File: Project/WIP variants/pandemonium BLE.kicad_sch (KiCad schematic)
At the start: 117 parts, among them J1 HRO_TYPE-C-31-M-14, J3 Battery, J7 TC2030_SWD, Q1 AO3407, SW1 RotaryEncoder_Switch, SW2 RotaryEncoder_Switch, U2 HOLYIOT-18010, U3 MCP73831, U4 USBLC6-2P6, U8 XC6206PxxxMR

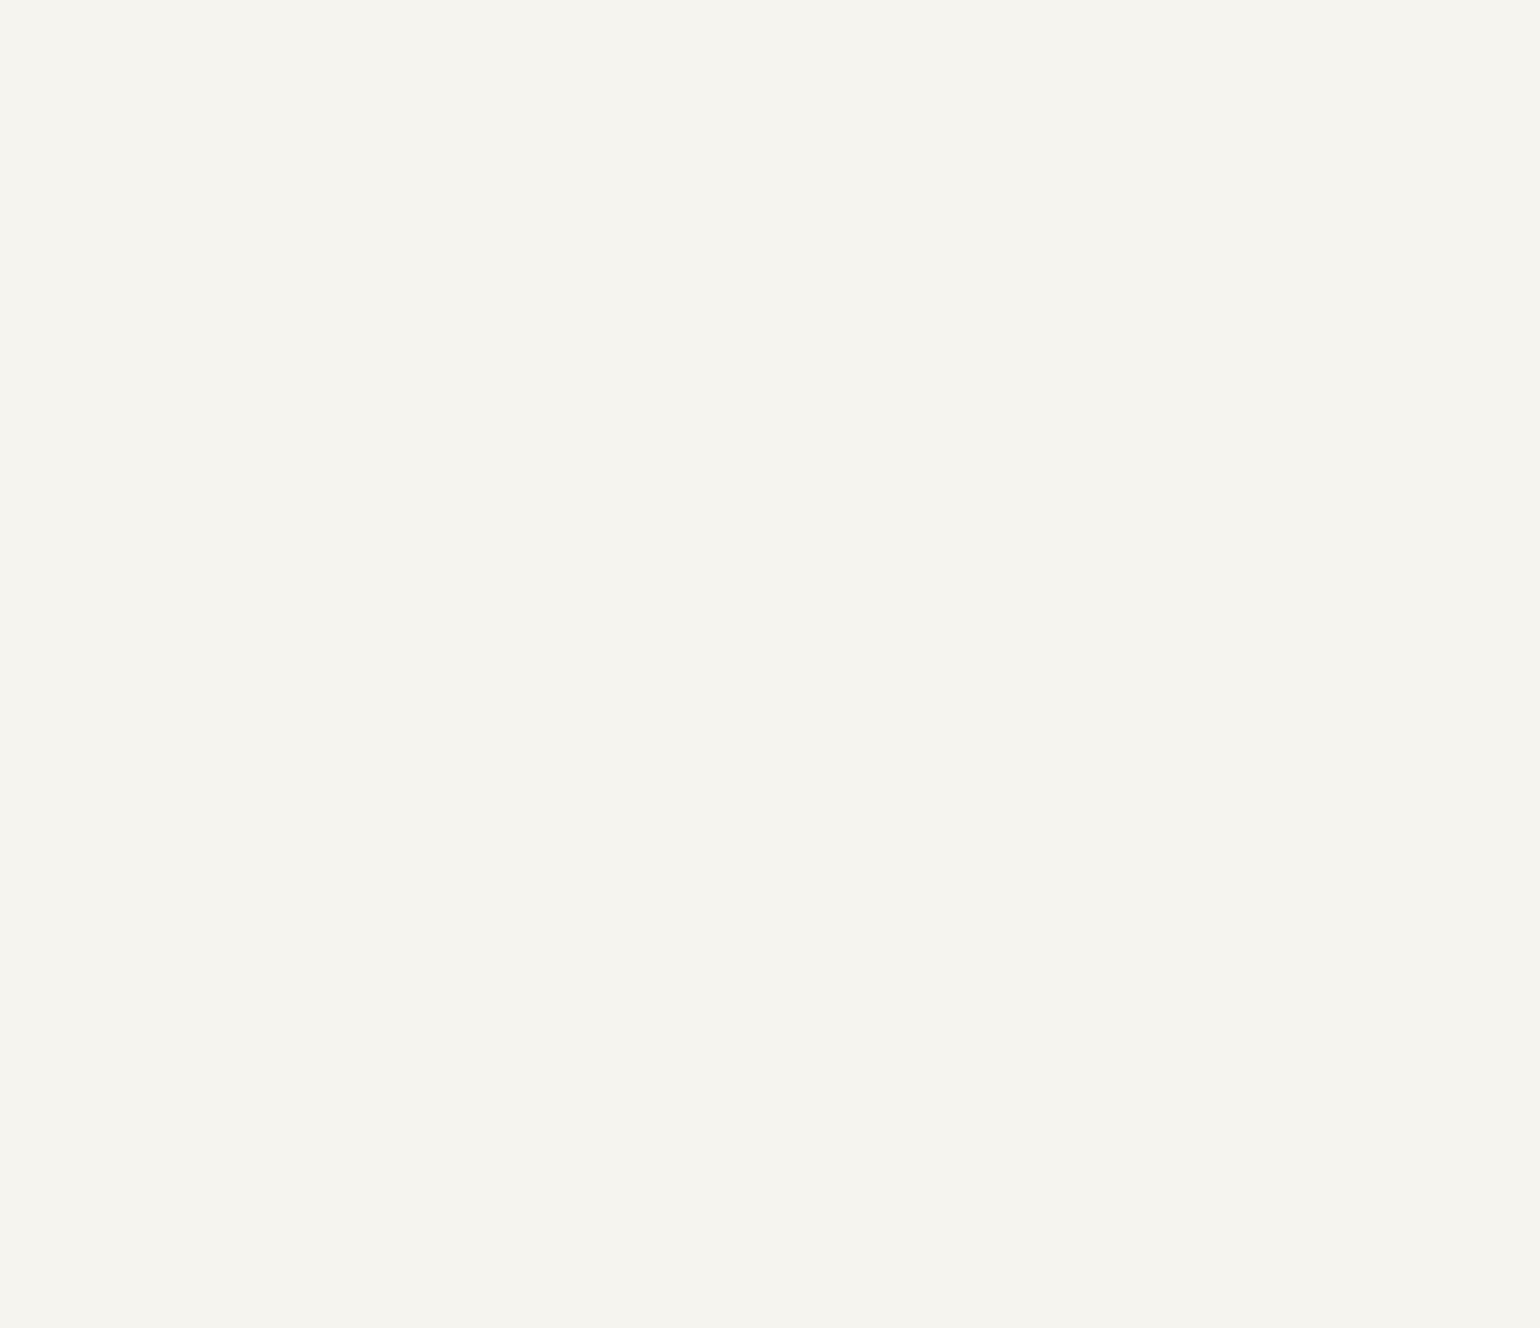
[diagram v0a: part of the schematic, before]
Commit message: e73 version work
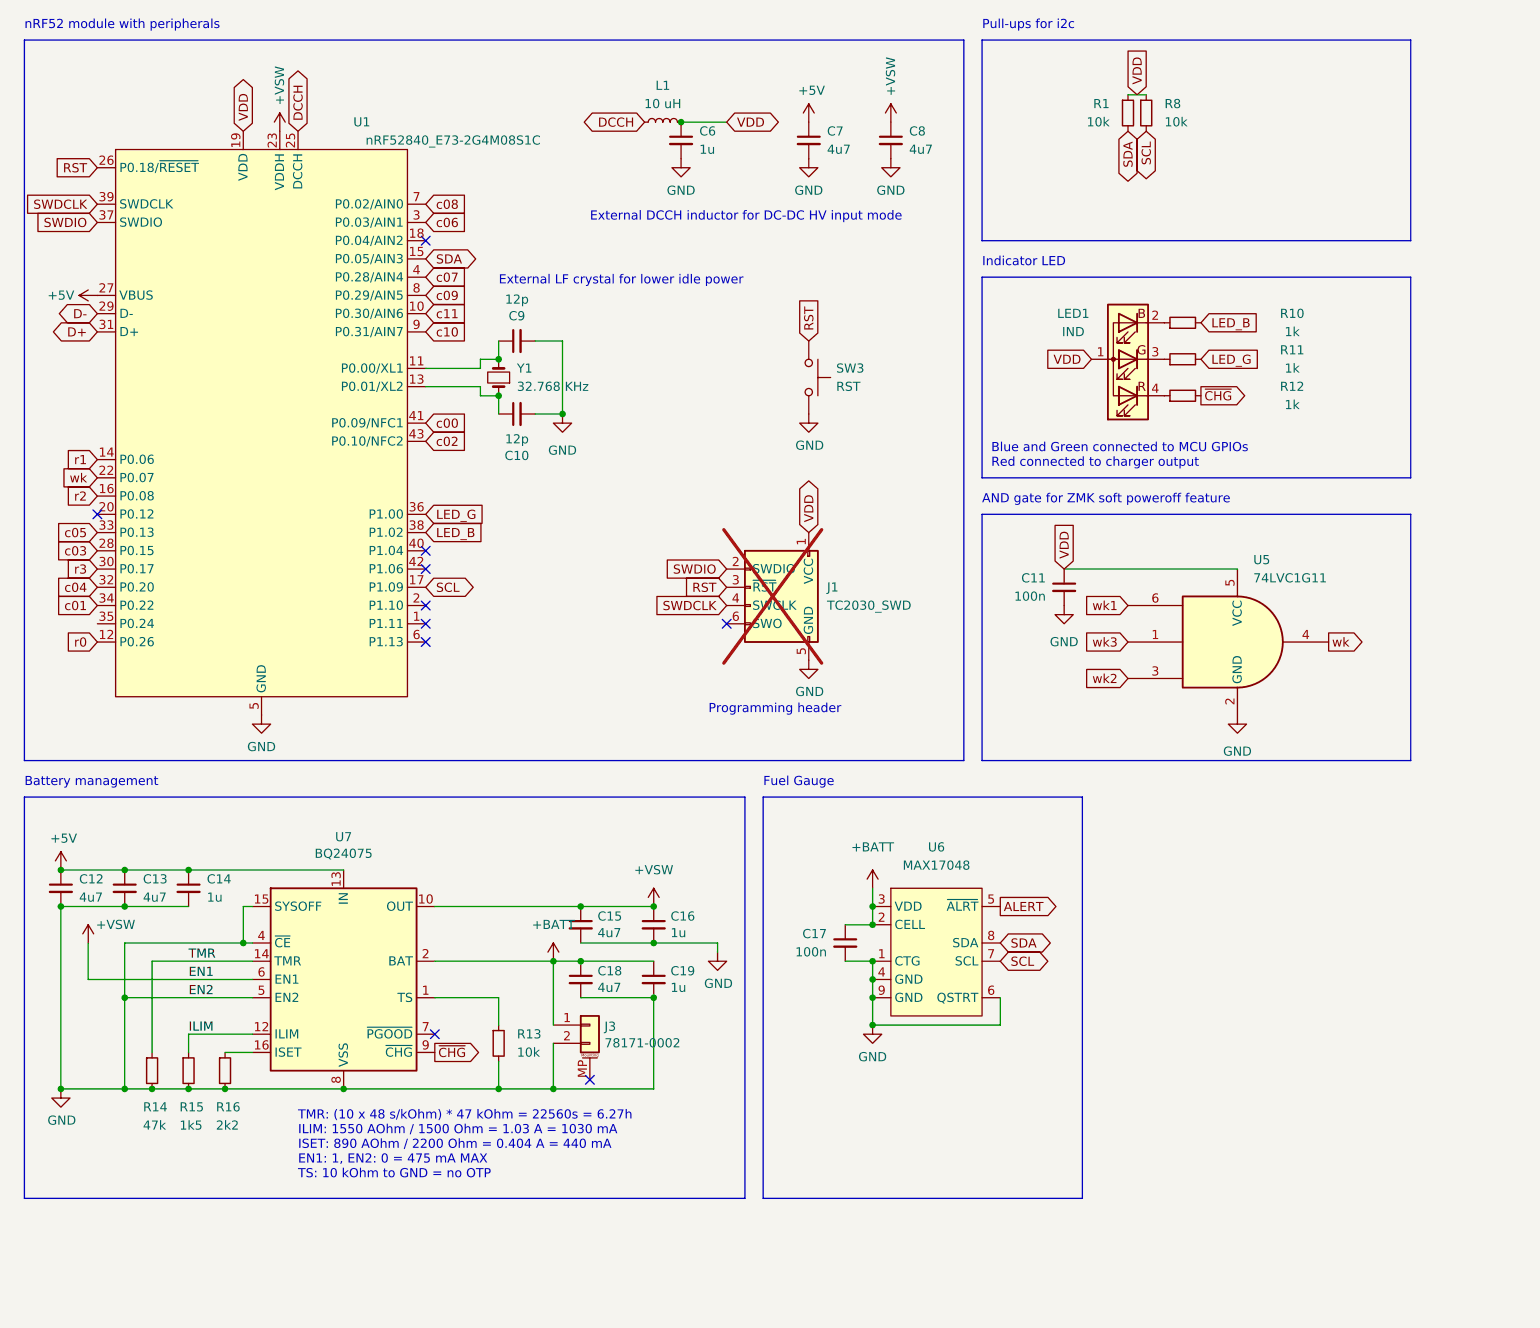
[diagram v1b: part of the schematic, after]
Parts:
- added C10, C9: 12p, Capacitor_SMD:C_0402_1005Metric, symbol Device:C_Small
- added C11, C17: 100n, Capacitor_SMD:C_0402_1005Metric, symbol Device:C_Small
- added C12, C13, C15, C18, C7, C8: 4u7, Capacitor_SMD:C_0402_1005Metric, symbol Device:C_Small
- added C14, C16, C19, C6: 1u, Capacitor_SMD:C_0402_1005Metric, symbol Device:C_Small
- added J1: TC2030_SWD, PCM_marbastlib-various:CON_TC2030_outlined, symbol PCM_marbastlib-various:TC2030_SWD
- added J3: 78171-0002, PCM_marbastlib-various:Molex_Pico-EZmate_78171-0002_1x02-1MP_P1.20mm_Vertical, symbol Connector_Generic_MountingPin:Conn_01x02_MountingPin
- added L1: 10 uH, Inductor_SMD:L_0603_1608Metric, symbol Device:L_Small
- added LED1: IND, PCM_marbastlib-various:LED_1206R, symbol PCM_marbastlib-various:LED_MHT151RGBCT
- added R1, R13, R8: 10k, Resistor_SMD:R_0402_1005Metric, symbol Device:R_Small
- added R10, R11, R12: 1k, Resistor_SMD:R_0402_1005Metric, symbol Device:R_Small
- added R14: 47k, Resistor_SMD:R_0402_1005Metric, symbol Device:R_Small
- added R15: 1k5, Resistor_SMD:R_0402_1005Metric, symbol Device:R_Small
- added R16: 2k2, Resistor_SMD:R_0402_1005Metric, symbol Device:R_Small
- added SW3: RST, PCM_marbastlib-various:SW_T1A2QR, symbol Switch:SW_Push
- added U1: nRF52840_E73-2G4M08S1C, PCM_marbastlib-various:nRF52840_E73-2G4M08S1C, symbol PCM_marbastlib-various:nRF52840_E73-2G4M08S1C
- added U5: 74LVC1G11, Package_TO_SOT_SMD:SOT-363_SC-70-6, symbol 74xGxx:74LVC1G11
- added U6: MAX17048, Package_DFN_QFN:DFN-8-1EP_2x2mm_P0.5mm_EP0.7x1.3mm, symbol marbastlib-various:MAX17048
- added U7: BQ24075, Package_DFN_QFN:VQFN-16-1EP_3x3mm_P0.5mm_EP1.6x1.6mm, symbol Battery_Management:BQ24075RGT
- added Y1: 32.768 KHz, Crystal:Crystal_SMD_2012-2Pin_2.0x1.2mm, symbol Device:Crystal_Small
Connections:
- net GND: now also C10.2, C11.2, C12.2, C13.2, C14.2, C15.2, C16.2, C17.2, C18.2, C19.2, C6.2, C7.2, C8.2, C9.2, J1.5 (GND), J3.2 (Pin_2), R13.2, R14.2, R15.2, R16.2, SW3.2, U1.21 (GND), U1.24 (GND), U1.5 (GND), U5.2 (GND), U6.1 (CTG), U6.4 (GND), U6.6 (QSTRT), U6.9 (GND), U7.15 (SYSOFF), U7.17 (VSS), U7.4 (~{CE}), U7.5 (EN2), U7.8 (VSS)
- net r1: now also U1.14 (P0.06)
- net r2: now also U1.16 (P0.08)
- new net: R13.1, U7.1 (TS)
- new net: LED1.2 (BK), R10.1
- new net: LED1.3 (GK), R11.1
- new net: LED1.4 (RK), R12.1
- new net: R16.1, U7.16 (ISET)
- new net: C9.1, U1.11 (P0.00/XL1), Y1.2
- new net: C10.1, U1.13 (P0.01/XL2), Y1.1
- new net +5V: C12.1, C13.1, C14.1, C7.1, U1.27 (VBUS), U7.13 (IN)
- new net +BATT: C17.1, C18.1, C19.1, J3.1 (Pin_1), U6.2 (CELL), U6.3 (VDD), U7.2 (BAT), U7.3 (BAT)
- new net +VSW: C15.1, C16.1, C8.1, U1.23 (VDDH), U7.10 (OUT), U7.11 (OUT), U7.6 (EN1)
- new net ALERT: U6.5 (~{ALRT})
- new net D+: U1.31 (D+)
- new net D-: U1.29 (D-)
- new net DCCH: L1.1, U1.25 (DCCH)
- new net ILIM: R15.1, U7.12 (ILIM)
- new net LED_B: R10.2, U1.38 (P1.02)
- new net LED_G: R11.2, U1.36 (P1.00)
- new net RST: J1.3 (~{RST}), SW3.1, U1.26 (P0.18/~{RESET})
- new net SCL: R8.2, U1.17 (P1.09), U6.7 (SCL)
- new net SDA: R1.2, U1.15 (P0.05/AIN3), U6.8 (SDA)
- new net SWDCLK: J1.4 (SWCLK), U1.39 (SWDCLK)
- new net SWDIO: J1.2 (SWDIO), U1.37 (SWDIO)
- new net TMR: R14.1, U7.14 (TMR)
- new net VDD: C11.1, C6.1, J1.1 (VCC), L1.2, LED1.1 (A), R1.1, R8.1, U1.19 (VDD), U5.5 (VCC)
- new net c00: U1.41 (P0.09/NFC1)
- new net c01: U1.34 (P0.22)
- new net c02: U1.43 (P0.10/NFC2)
- new net c03: U1.28 (P0.15)
- new net c04: U1.32 (P0.20)
- new net c05: U1.33 (P0.13)
- new net c06: U1.3 (P0.03/AIN1)
- new net c07: U1.4 (P0.28/AIN4)
- new net c08: U1.7 (P0.02/AIN0)
- new net c09: U1.8 (P0.29/AIN5)
- new net c10: U1.9 (P0.31/AIN7)
- new net c11: U1.10 (P0.30/AIN6)
- new net r0: U1.12 (P0.26)
- new net r3: U1.30 (P0.17)
- new net wk: U1.22 (P0.07), U5.4
- new net wk1: U5.6
- new net wk2: U5.3
- new net wk3: U5.1
- new net ~{CHG}: R12.2, U7.9 (~{CHG})
- no-connect marks 3 -> 13
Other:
- note added: "AND gate for ZMK soft poweroff feature"
- note added: "Battery management"
- note added: "Blue and Green connected to MCU GPIOs Red connected to charger output"
- note added: "External DCCH inductor for DC-DC HV input mode"
- note added: "External LF crystal for lower idle power"
- note added: "Fuel Gauge"
- note added: "Indicator LED"
- note added: "Programming header"
- note added: "Pull-ups for i2c"
- note added: "TMR: (10 x 48 s/kOhm) * 47 kOhm = 22560s = 6.27h ILIM: 1550 AOhm / 1500 Ohm = 1.03 A = 1030 mA ISET: 890 AOhm / 2200 Ohm = 0.404 A = 440 mA EN1: 1, EN2: 0 = 475 mA MAX TS: 10 kOhm to GND = no OTP"
- note added: "nRF52 module with peripherals"
